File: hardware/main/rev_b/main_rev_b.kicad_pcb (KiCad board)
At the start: 4 copper layers, 140 x 100 mm, 165 parts, among them J1 USB-C USB2, J10 SWD, J2 ESC_CAN_POWER, J30 GNSS_UFL, J40 915MHz_ANT, Q30 2N7002, U1 USBLC6-2SC6, U10 RP2354B, U2 TLV62569DBVR, U20 ICM-42688-P, U21 LSM6DSO32TR, U22 LPS22DFTR, U3 TLV75528PDBVR, U30 LG77LICMD, U4 TLV75533PDBVR, U40 CC1121RHBR, U41 CC1190RGVR, U50 TCAN3413DR, U51 MCP2518FD-H/QBB, Y1 12MHz ABM8-272-T3, Y40 32MHz NT2016SA-32M-TEE3017A, Y50 40MHz ABM8G

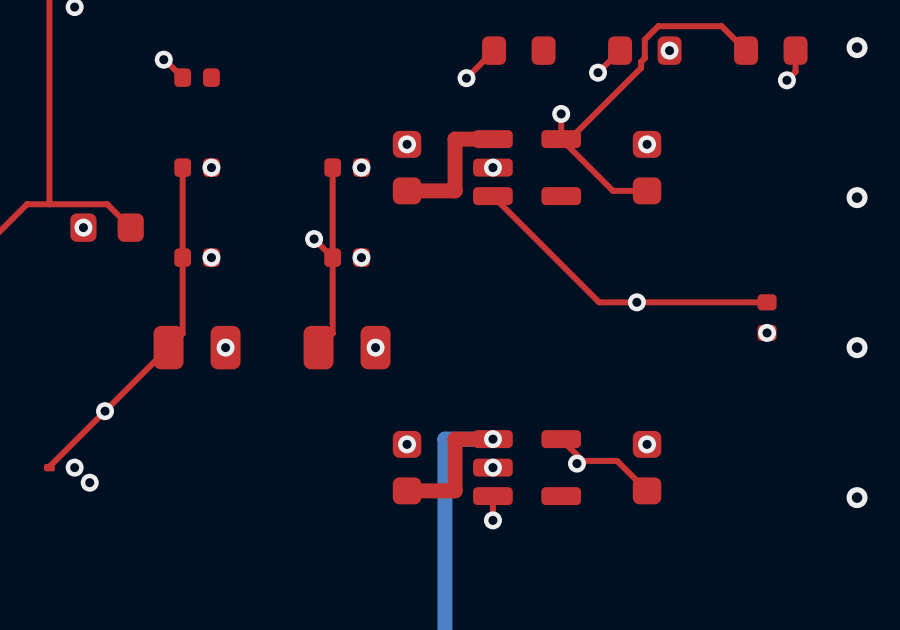
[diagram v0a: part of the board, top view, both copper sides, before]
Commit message: pcb: connect local rev b sys5v input island
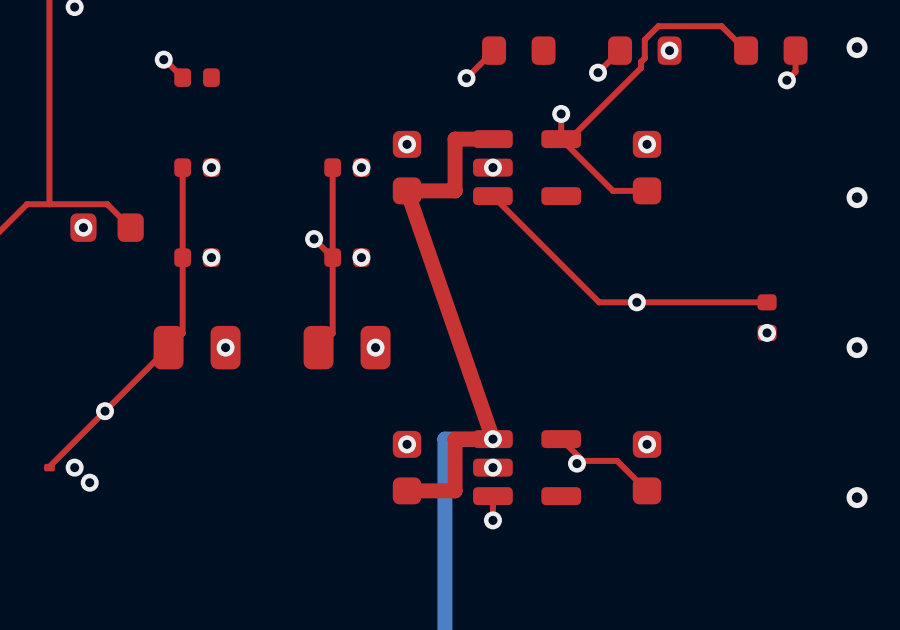
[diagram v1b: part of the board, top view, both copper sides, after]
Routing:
- net /SYS_5V: track 178.0 -> 186.7 mm
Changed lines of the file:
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@@
+	)
+	(segment
+		(start 122 17.775)
+		(end 124.8625 26.05)
+		(width 0.5)
+		(layer "F.Cu")
+		(net 107)
 	)
 	(segment

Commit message: pcb: connect local rev b u2 sys5v branch
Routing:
- net /SYS_5V: track 186.7 -> 190.8 mm, vias 2 -> 3
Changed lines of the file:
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@@
+		(net 107)
+	)
+	(via
+		(at 27.8625 73.6)
+		(size 0.6)
+		(drill 0.3)
+		(layers "F.Cu" "B.Cu")
 		(net 107)
 	)
@@
 		(width 0.5)
 		(layer "B.Cu")
+		(net 107)
+	)
+	(segment
+		(start 27.8625 73.6)
+		(end 30.1375 76.95)
+		(width 0.5)
+		(layer "B.Cu")

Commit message: pcb: route local rev b r4 1v1 link
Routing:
- net /1V1: track 1.55 -> 7.15 mm
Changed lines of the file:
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@@
+		(net 1)
+	)
+	(segment
+		(start 50.49 41.5)
+		(end 51.52 47)
+		(width 0.2)
+		(layer "F.Cu")
 		(net 1)
 	)

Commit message: pcb: route rev b status led signal
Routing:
- net /RP2354B MCU/STATUS_LED: track 0.00 -> 17.1 mm
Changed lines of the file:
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@@
+	)
+	(segment
+		(start 53.3 59.5)
+		(end 52.41 60.1)
+		(width 0.2)
+		(layer "F.Cu")
+		(net 96)
+	)
+	(segment
+		(start 63.8 55.95)
+		(end 64.5 56.65)
+		(width 0.2)
+		(layer "F.Cu")
+		(net 96)
+	)
+	(segment
+		(start 64.5 56.65)
+		(end 64.5 58)
+		(width 0.2)
+		(layer "F.Cu")
+		(net 96)
+	)
+	(segment
+		(start 62.8 54.95)
+		(end 63.8 55.95)
+		(width 0.2)
+		(layer "F.Cu")
+		(net 96)
+	)
+	(segment
+		(start 53.8 58)
+		(end 53.3 59.5)
+		(width 0.2)
+		(layer "F.Cu")
+		(net 96)
+	)
+	(segment
+		(start 64.5 58)
+		(end 53.8 58)
+		(width 0.2)
+		(layer "F.Cu")
+		(net 96)
 	)
 	(segment

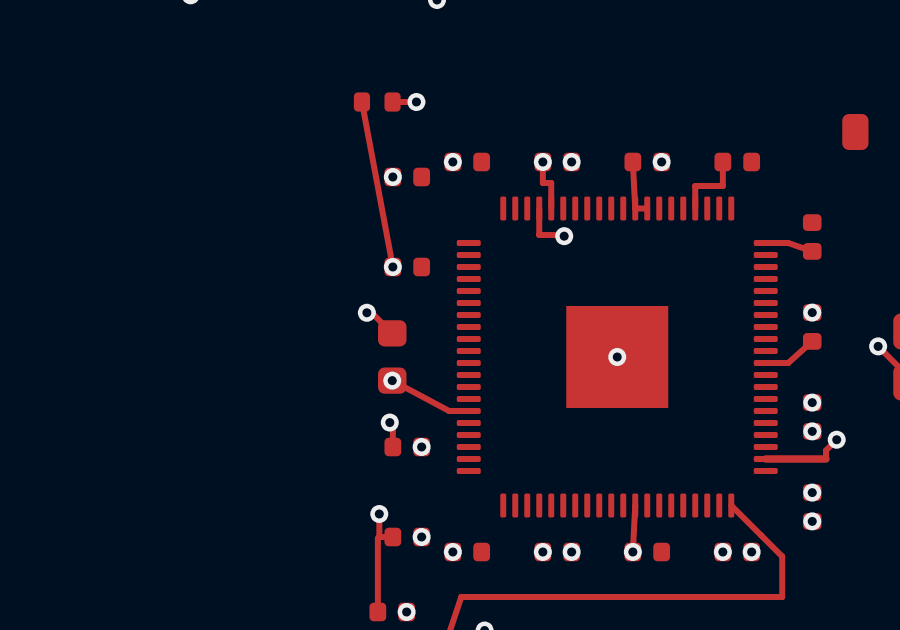
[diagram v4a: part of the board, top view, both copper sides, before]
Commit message: pcb: route rev b baro scl escape via inner layer
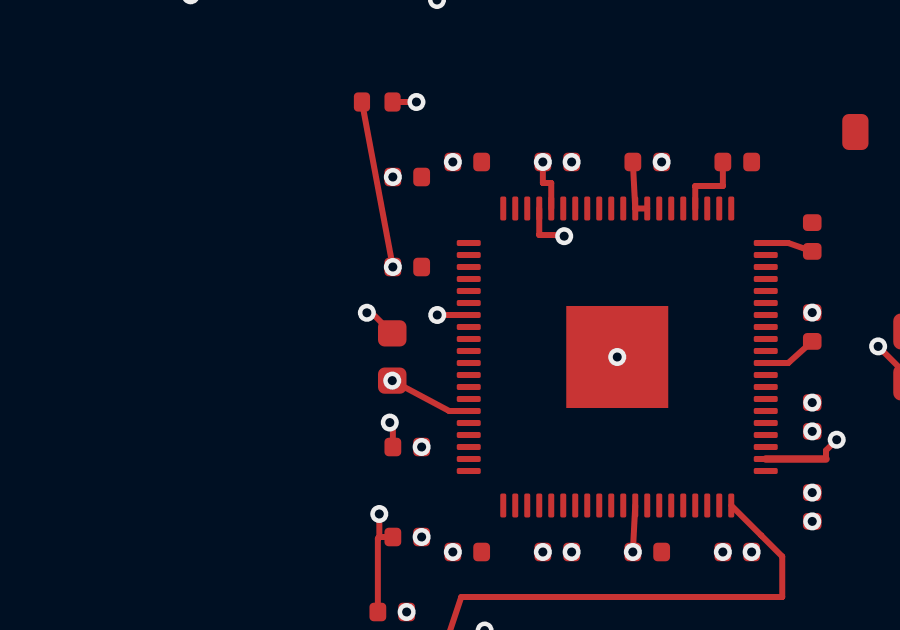
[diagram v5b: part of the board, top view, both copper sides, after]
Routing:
- net /BARO_SCL: track 8.80 -> 51.5 mm, vias 2 -> 3
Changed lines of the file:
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@@
+	)
+	(segment
+		(start 54.05 48.6)
+		(end 53 48.6)
+		(width 0.2)
+		(layer "F.Cu")
+		(net 39)
 	)
 	(segment
@@
 		(width 0.2)
 		(layer "F.Cu")
+		(net 39)
+	)
+	(via
+		(at 53 48.6)
+		(size 0.6)
+		(drill 0.3)
+		(layers "F.Cu" "B.Cu")
 		(net 39)
 	)
@@
 		(net 39)
 	)
+	(segment
+		(start 66.8 79.2)
+		(end 66.8 80.8)
+		(width 0.2)
+		(layer "In2.Cu")
+		(net 39)
+	)
+	(segment
+		(start 64.599999 77)
+		(end 66.8 79.2)
+		(width 0.2)
+		(layer "In2.Cu")
+		(net 39)
+	)
+	(segment
+		(start 68.7126 82.7126)
+		(end 68.7126 83.7749)
+		(width 0.2)
+		(layer "In2.Cu")
+		(net 39)
+	)
+	(segment
+		(start 54.8 57.2)
+		(end 64.599999 67)
+		(width 0.2)
+		(layer "In2.Cu")
+		(net 39)
+	)
+	(segment
+		(start 64.599999 67)
+		(end 64.599999 77)
+		(width 0.2)
+		(layer "In2.Cu")
+		(net 39)
+	)
+	(segment
+		(start 53 48.6)
+		(end 54.8 50.4)
+		(width 0.2)
+		(layer "In2.Cu")
+		(net 39)
+	)
+	(segment
+		(start 54.8 50.4)
+		(end 54.8 57.2)
+		(width 0.2)
+		(layer "In2.Cu")
+		(net 39)
+	)
+	(segment
+		(start 66.8 80.8)
+		(end 68.7126 82.7126)
+		(width 0.2)
+		(layer "In2.Cu")
+		(net 39)
+	)

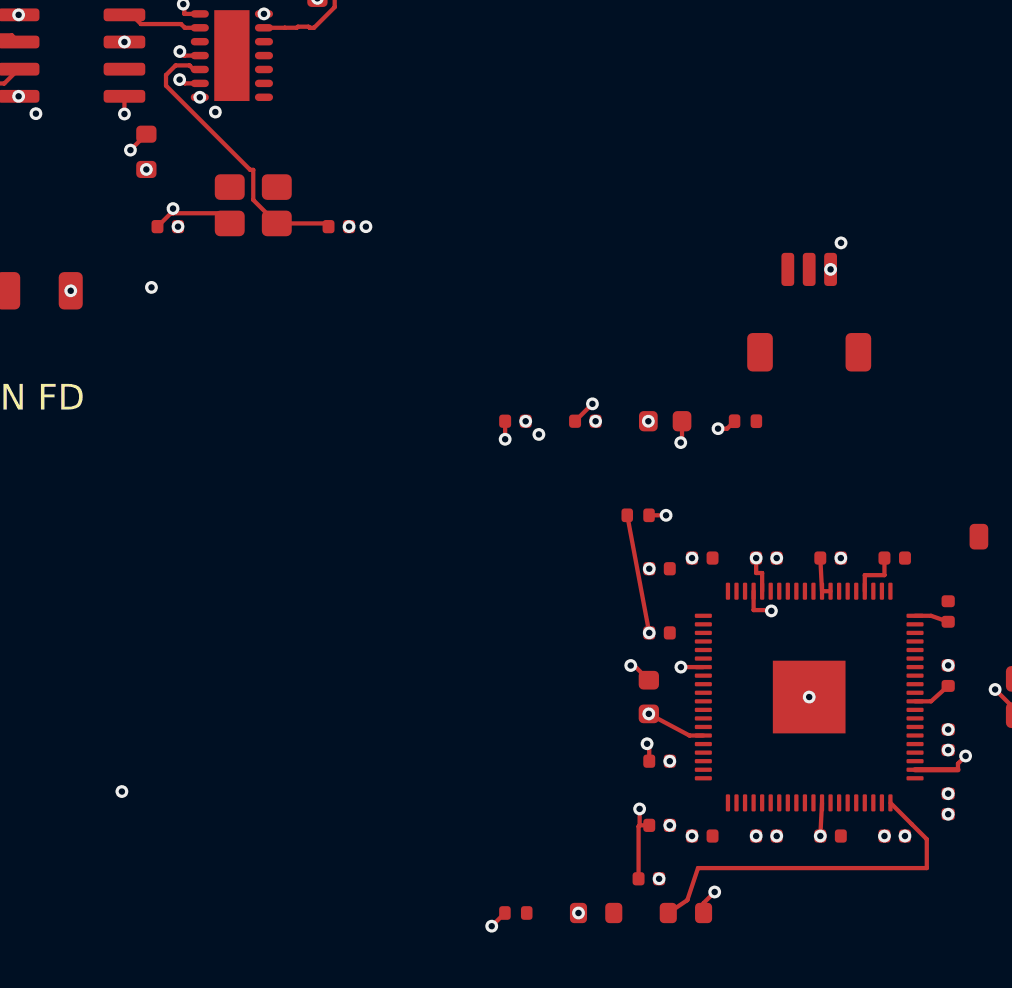
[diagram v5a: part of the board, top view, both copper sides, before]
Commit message: pcb: route rev b CAN interrupt on back copper
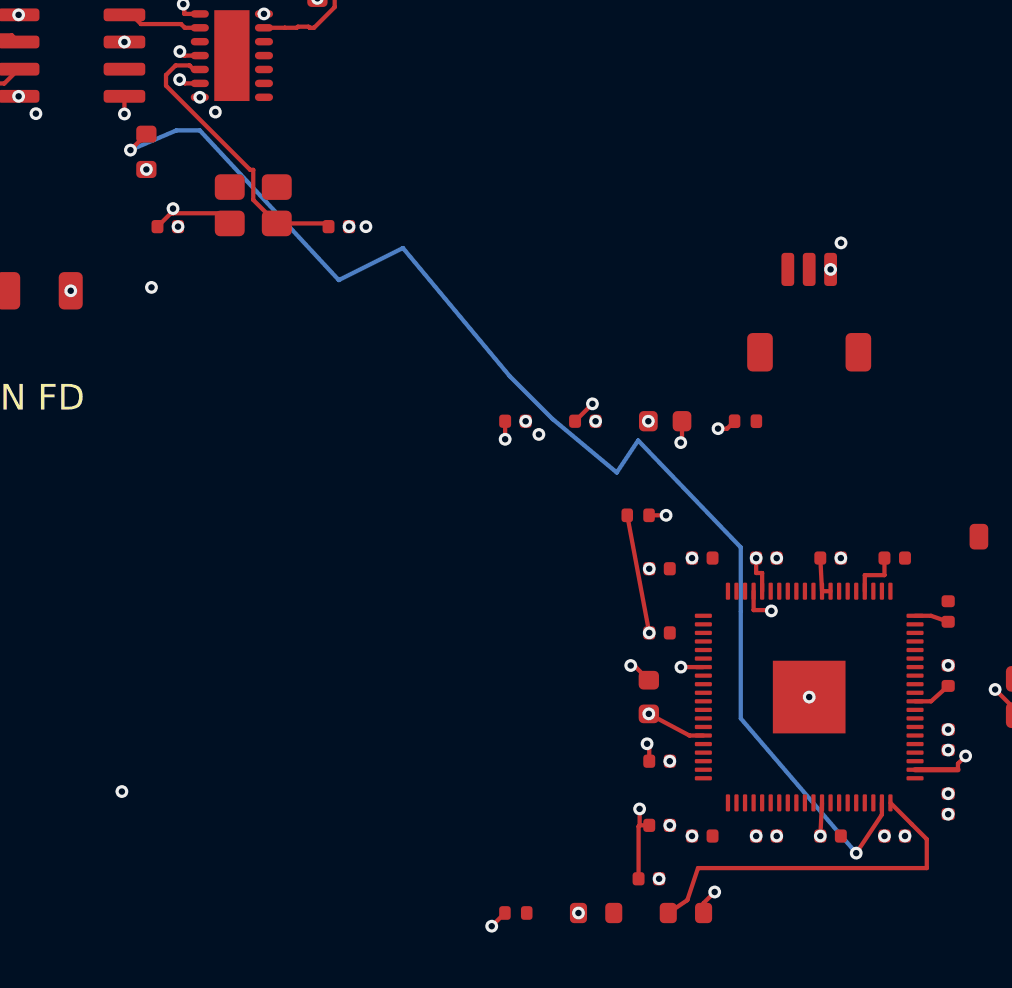
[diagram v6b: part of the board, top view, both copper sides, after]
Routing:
- net /CAN_INT: track 7.63 -> 66.3 mm, vias 2 -> 3
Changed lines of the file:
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@@
+	)
+	(segment
+		(start 62.4 55.5)
+		(end 61.2 57.3)
+		(width 0.2)
+		(layer "F.Cu")
+		(net 51)
 	)
 	(segment
@@
 		(net 51)
 	)
+	(segment
+		(start 62.4 54.95)
+		(end 62.4 55.5)
+		(width 0.2)
+		(layer "F.Cu")
+		(net 51)
+	)
 	(via
 		(at 27.2547 24.4203)
@@
 		(net 51)
 	)
+	(via
+		(at 61.2 57.3)
+		(size 0.6)
+		(drill 0.3)
+		(layers "F.Cu" "B.Cu")
+		(net 51)
+	)
+	(segment
+		(start 47 37)
+		(end 45 35)
+		(width 0.2)
+		(layer "B.Cu")
+		(net 51)
+	)
+	(segment
+		(start 50 39.5)
+		(end 47 37)
+		(width 0.2)
+		(layer "B.Cu")
+		(net 51)
+	)
+	(segment
+		(start 51 38)
+		(end 50 39.5)
+		(width 0.2)
+		(layer "B.Cu")
+		(net 51)
+	)
+	(segment
+		(start 37 30.5)
+		(end 30.5 23.5)
+		(width 0.2)
+		(layer "B.Cu")
+		(net 51)
+	)
+	(segment
+		(start 55.8 51)
+		(end 55.8 46)
+		(width 0.2)
+		(layer "B.Cu")
+		(net 51)
+	)
+	(segment
+		(start 29.4 23.5)
+		(end 27.2547 24.4203)
+		(width 0.2)
+		(layer "B.Cu")
+		(net 51)
+	)
+	(segment
+		(start 55.8 43)
+		(end 51 38)
+		(width 0.2)
+		(layer "B.Cu")
+		(net 51)
+	)
+	(segment
+		(start 55.8 46)
+		(end 55.8 43)
+		(width 0.2)
+		(layer "B.Cu")
+		(net 51)
+	)
+	(segment
+		(start 30.5 23.5)
+		(end 29.4 23.5)
+		(width 0.2)
+		(layer "B.Cu")
+		(net 51)
+	)
+	(segment
+		(start 45 35)
+		(end 40 29)
+		(width 0.2)
+		(layer "B.Cu")
+		(net 51)
+	)
+	(segment
+		(start 40 29)
+		(end 37 30.5)
+		(width 0.2)
+		(layer "B.Cu")
+		(net 51)
+	)
+	(segment
+		(start 61.2 57.3)
+		(end 55.8 51)
+		(width 0.2)
+		(layer "B.Cu")
+		(net 51)
+	)
